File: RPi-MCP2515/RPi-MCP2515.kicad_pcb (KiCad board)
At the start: 2 copper layers, 65 x 56.5 mm, 47 parts, among them P1 CONN_02X20, P10 CONN_02X08, P11 CONN_02X08, P12 CONN_01X08, P13 CONN_02X08, P14 CONN_02X08, P15 CONN_01X06, P16 DCDC 5V, P2 CONN_01X02, P3 CONN_01X03, P4 CONN_01X09, P5 CONN_01X04, P6 CONN_01X02, P7 CONN_01X04, P8 CONN_01X02, P9 CONN_01X04, U1 MCP2515, U2 MCP2562, U6 ISO1050, U7 LM7805, U8 P82B715, Y1 16MHz

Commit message: update
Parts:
- removed R6: var, w_pth_resistors:RC03
- added G***: LOGO, w_logo:Logo_copper_CC-BY-NC-SA_10x3.6mm, F.Cu at (169.4, 125.9)
- P7: value CONN_01X04 -> CONN_01X05; footprint w_conn_pt-1,5:pt_1,5-4-3,5-h -> w_conn_pt-1,5:pt_1,5-5-3,5-h
- moved C6 7.62 mm to (151.8, 117.5), turned to 90 degrees
- moved C7 6.35 mm to (151.8, 110.5), turned to 270 degrees
- moved P7 2.01 mm to (149.2, 125.1)
- moved D1 1.91 mm to (138.4, 124.5)
- moved R5 1.91 mm to (136.5, 120.7)
- moved C9 0.63 mm to (154.9, 119.4)
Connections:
- P7 pad 1: +5VA -> GNDA
- P7 pad 2: Net-(P7-Pad2) -> Net-(P6-Pad2)
- P7 pad 3: Net-(P6-Pad2) -> Net-(P7-Pad3)
- P7 pad 4: GNDA -> +5VA
- R13 pad 2: Net-(P7-Pad2) -> Net-(P7-Pad3)
- U6 pad 7: Net-(P7-Pad2) -> Net-(P7-Pad3)
- U7 pad 1: (no net) -> +5VA
- U7 pad 2: (no net) -> GNDA
- U7 pad 3: (no net) -> VCOM
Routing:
- net +3V3: track 0.00 -> 178.8 mm
- net +5VA: track 0.00 -> 111.6 mm, vias 0 -> 1
- net GND: track 0.00 -> 103.8 mm, vias 0 -> 9
- net +5V: track 0.00 -> 91.2 mm, vias 0 -> 1
- net GNDA: track 0.00 -> 74.7 mm, vias 0 -> 4
- net /GPIO4: track 8.67 -> 70.4 mm, vias 0 -> 2
- net /RxD: track 0.00 -> 60.9 mm
- net /TxD: track 0.00 -> 59.5 mm
- net /SDA: track 0.00 -> 53.9 mm, vias 0 -> 1
- net /GPIO17: track 8.67 -> 60.4 mm, vias 0 -> 2
- net /SCL: track 0.00 -> 50.2 mm
- net Net-(P2-Pad2): track 0.00 -> 44.3 mm
- net /GPIO21: track 8.67 -> 51.2 mm, vias 0 -> 3
- net /GPIO22: track 8.67 -> 48.5 mm, vias 0 -> 2
- net Net-(P3-Pad1): track 0.00 -> 36.9 mm
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- added copper zone on B.Cu, net GND
- added copper zone on F.Cu, net GND
- added copper zone on B.Cu, net GNDA
- added copper zone on F.Cu, net GNDA
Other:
- net class PWRII added: clearance 0.2, trace_width 1.16, via_dia 1.2, via_drill 1
- board text added: "CH"
- board text added: "CL"
- board text added: "RPi-CAN/I2C V1.0 Gerhard Bertelsmann"
- board text added: "T"
- board text added: "VCOM"

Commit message: add some pictures
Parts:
- moved C7 7.49 mm to (151.9, 118.0), turned to 90 degrees
- moved C6 6.48 mm to (151.9, 111.0), turned to 270 degrees
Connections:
- U7 pad 1: +5VA -> VCOM
- U7 pad 3: VCOM -> +5VA
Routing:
- net +5VA: track 111.6 -> 100.1 mm
- net VCOM: track 15.9 -> 19.8 mm

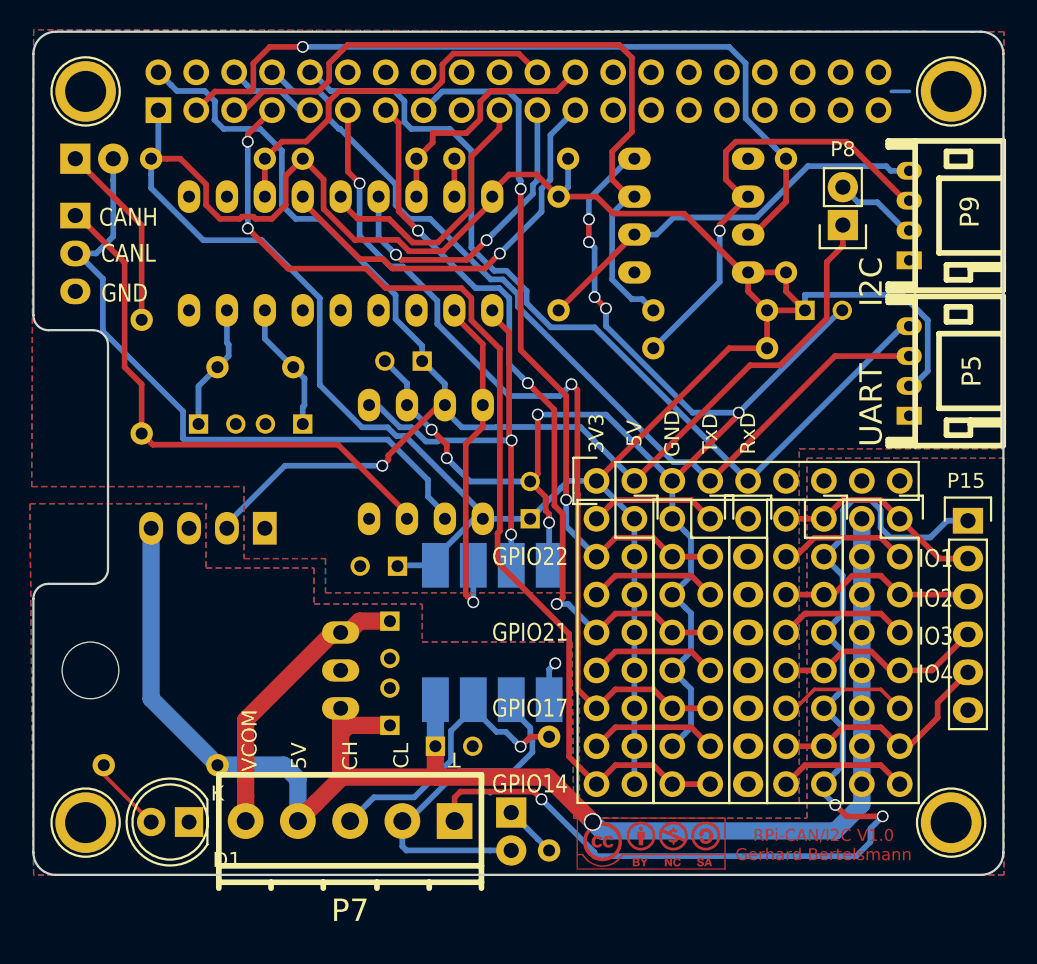
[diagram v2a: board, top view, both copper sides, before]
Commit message: move C3 closer to CAN Cpntroller
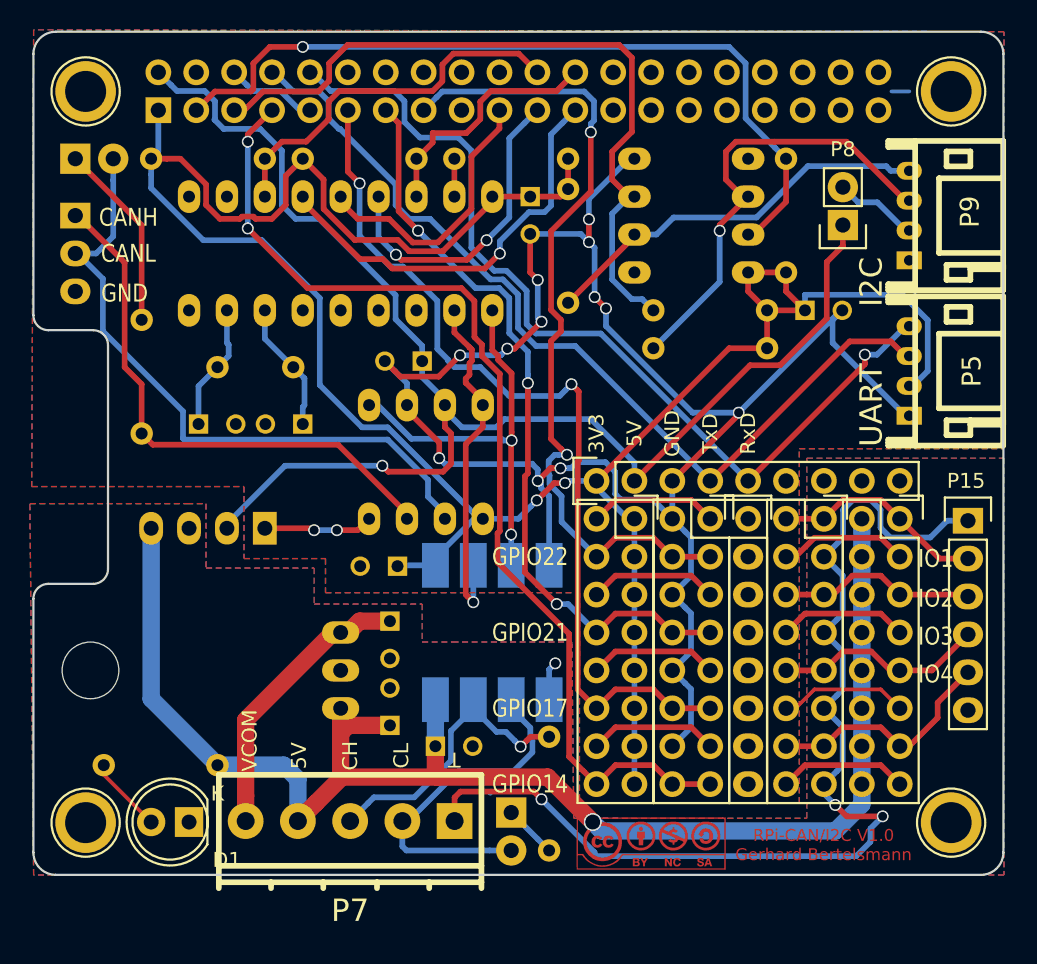
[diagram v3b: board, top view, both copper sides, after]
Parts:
- moved C3 21.6 mm to (161.3, 82.5), turned to 270 degrees
- moved R14 0.81 mm to (163.8, 85.9)
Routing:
- net GND: track 103.8 -> 141.3 mm, vias 9 -> 14
- net +3V3: track 178.8 -> 163.6 mm, vias 0 -> 2
- net /GPIO22: track 48.5 -> 55.9 mm
- net +5V: track 91.2 -> 95.4 mm
- net /TxD: track 59.5 -> 61.1 mm
- net /RxD: track 60.9 -> 62.5 mm, vias 0 -> 1
- net /GPIO17: track 60.4 -> 61.5 mm
- net Net-(P9-Pad4): track 27.6 -> 26.9 mm
- net Net-(U1-Pad2): track 23.5 -> 24.2 mm
- net /SCK: track 27.5 -> 28.1 mm

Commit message: prepare 1.1
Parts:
- added P17: PWR, Pin_Headers:Pin_Header_Straight_1x02, F.Cu at (191.4, 120.3)
- R5: value 120 -> 1k5
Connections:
- net /GPIO21 renamed /GPIO27
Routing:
- net +5VA: track 100.1 -> 107.8 mm
- net VCC: track 0.00 -> 3.69 mm
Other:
- board text added: "GPIO27"
- board text added: "GPIO4"
- board text added: "RPi-CAN/I2C V1.1 Gerhard Bertelsmann"
- board text removed: "GPIO14"
- board text removed: "GPIO21"
- board text removed: "RPi-CAN/I2C V1.0 Gerhard Bertelsmann"

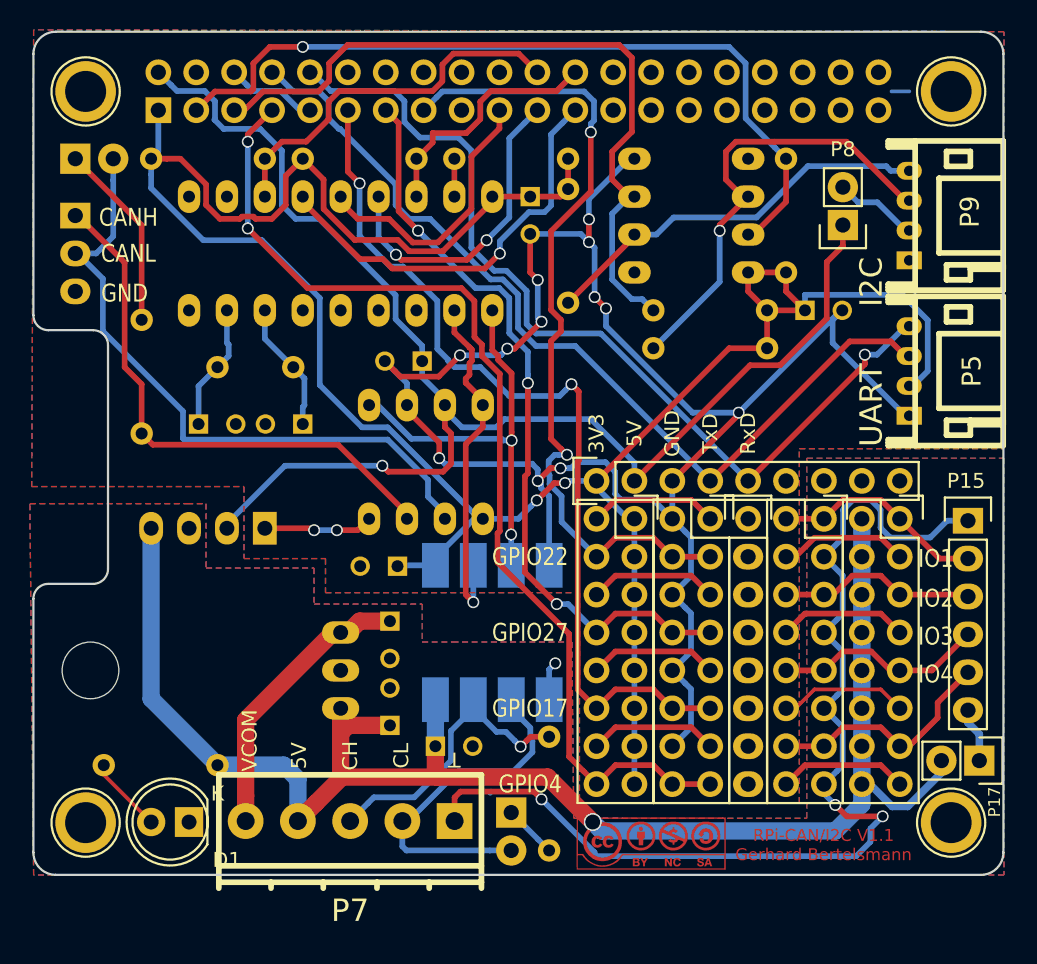
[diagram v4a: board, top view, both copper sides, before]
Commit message: fix I2C bus extender
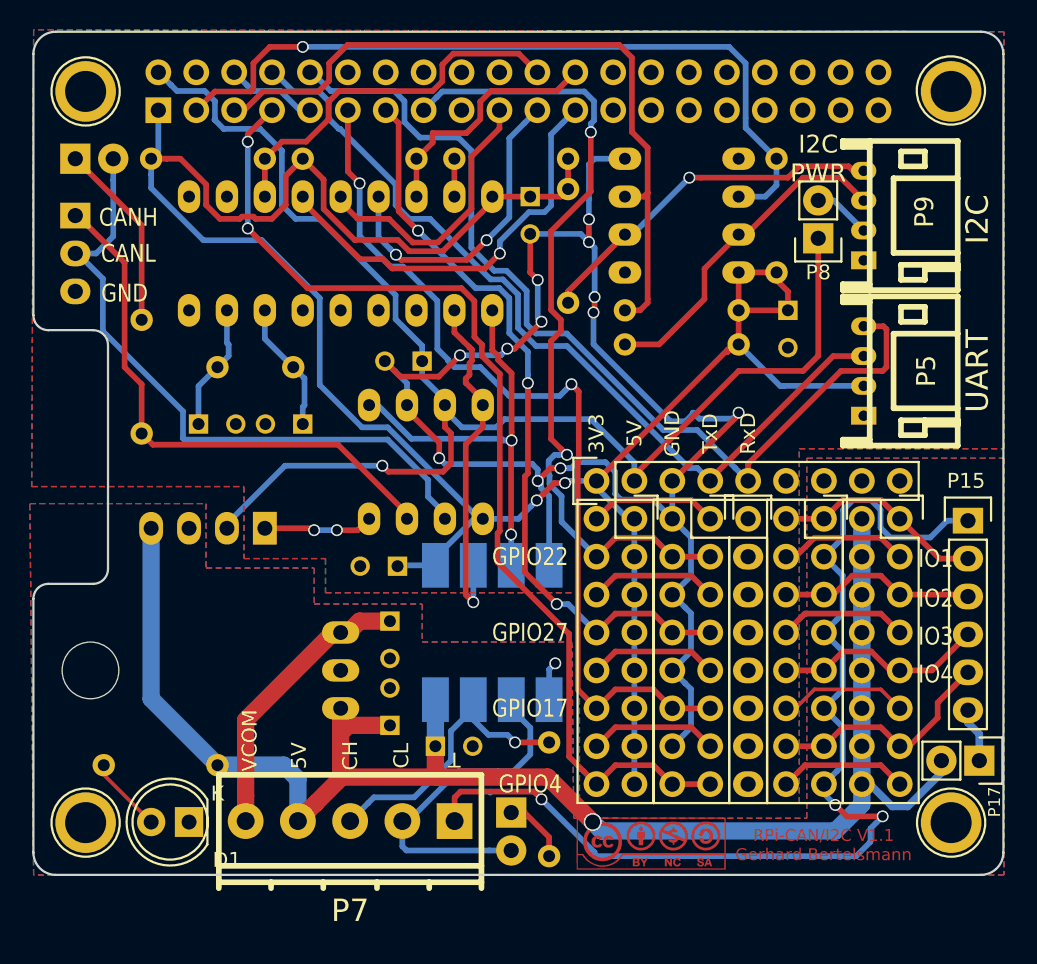
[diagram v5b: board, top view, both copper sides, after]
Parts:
- removed U8: P82B715, w_pth_circuits:dil_8-300_socket
- added U3: P82B715, w_pth_circuits:dil_8-300_socket, B.Cu at (171.4, 83.8)
- moved P5 3.05 mm to (183.6, 94.2)
- moved P9 3.05 mm to (183.6, 83.8)
- moved R15 1.92 mm to (171.4, 92.5)
- moved R25 1.91 mm to (171.4, 90.2)
- moved P8 1.88 mm to (180.6, 85.3)
- moved C4 1.14 mm to (178.6, 90.2), turned to 270 degrees
- moved R24 0.63 mm to (177.8, 83.8)
- moved R13 0.38 mm to (162.6, 122.9)
- moved REF** 0.06 mm to (189.5, 75.4)
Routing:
- net GND: track 141.3 -> 124.9 mm
- net Net-(P9-Pad3): track 30.8 -> 22.5 mm, vias 1 -> 0
- net +3V3: track 163.6 -> 156.1 mm
- net /TxD: track 61.1 -> 57.7 mm
- net Net-(P9-Pad4): track 26.9 -> 24.2 mm, vias 0 -> 1
- net Net-(P8-Pad2): track 5.65 -> 3.88 mm
- net /RxD: track 62.5 -> 63.9 mm, vias 1 -> 0
- net /SDA: track 53.9 -> 52.6 mm
- net (no net): track 1.31 -> 0.11 mm
- net Net-(P6-Pad1): track 3.59 -> 4.49 mm
- net Net-(P7-Pad3): track 20.6 -> 21.2 mm
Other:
- board text added: "I2C PWR"

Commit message: V1.1
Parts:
- moved P17 45.4 mm to (146.1, 116.9), turned to 0 degrees
- moved P15 0.52 mm to (191.1, 104.1)
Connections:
- P14 pad 10: +5VA -> Net-(P14-Pad10)
- P14 pad 12: +5VA -> Net-(P14-Pad10)
- P14 pad 14: +5VA -> Net-(P14-Pad10)
- P14 pad 16: +5VA -> Net-(P14-Pad10)
- P14 pad 2: +5VA -> Net-(P14-Pad10)
- P14 pad 4: +5VA -> Net-(P14-Pad10)
- P14 pad 6: +5VA -> Net-(P14-Pad10)
- P14 pad 8: +5VA -> Net-(P14-Pad10)
- P15 pad 6: VCC -> Net-(P14-Pad10)
- P17 pad 1: VCC -> +5VA
- P17 pad 2: +5VA -> Net-(P14-Pad10)
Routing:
- net Net-(P14-Pad10): track 0.00 -> 71.8 mm, vias 0 -> 1
- net +5VA: track 107.8 -> 45.4 mm, vias 1 -> 0
- net VCC: track 3.69 -> 0.00 mm
- net VCOM: track 19.8 -> 21.9 mm
- net /IO4: track 15.9 -> 16.7 mm
- net /IO3: track 14.2 -> 14.8 mm
- net /IO1: track 14.3 -> 14.9 mm
- net GNDA: track 74.7 -> 75.2 mm
